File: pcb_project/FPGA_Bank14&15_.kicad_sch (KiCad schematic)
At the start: 16 parts, among them U1 XC7A100T-FTG256

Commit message: LED & FPGA_Started
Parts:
- removed C26: 330µF, symbol Device:C
- removed C27, C28, C29, C30, C31, C32: 4.7µF, symbol Device:C
- removed C33, C34, C35, C36, C37, C38, C39, C40: 0.47µF, symbol Device:C
- removed U1: XC7A100T-FTG256, symbol FPGA_Xilinx_Artix7:XC7A100T-FTG256
- added U7: XC7A100T-FTG256, symbol FPGA_Xilinx_Artix7:XC7A100T-FTG256
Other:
- removed sheet A_Bank14&15
- removed sheet B_Bank34&35

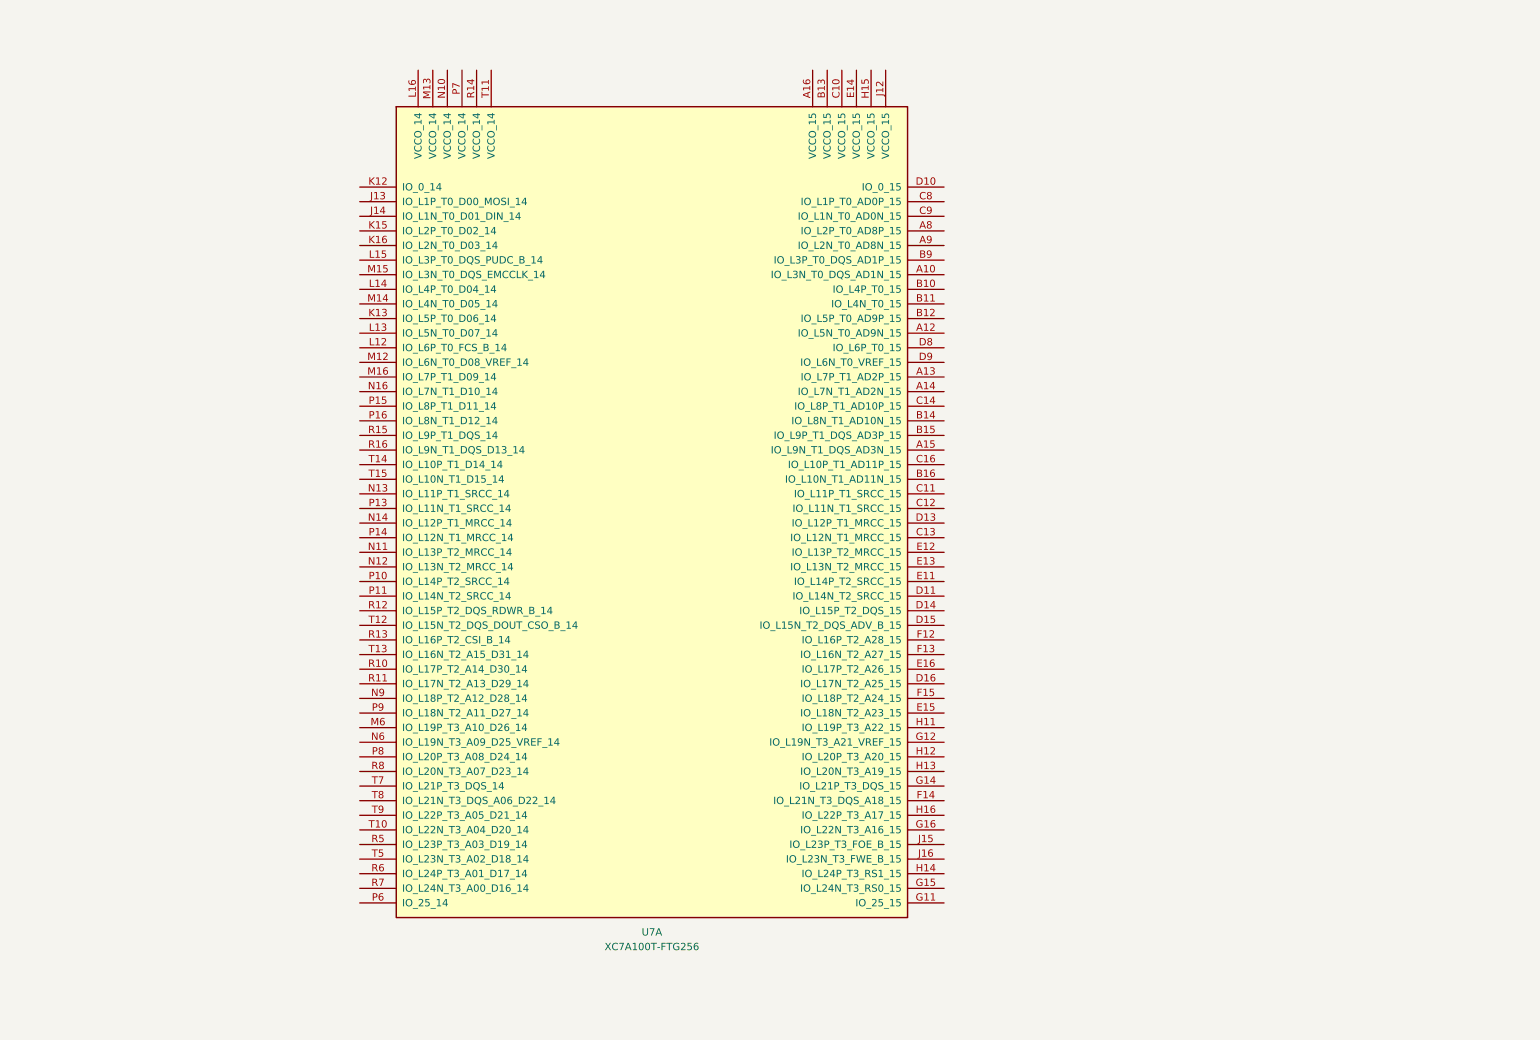
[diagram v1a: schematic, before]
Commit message: Crystal + SPI flash FPGA
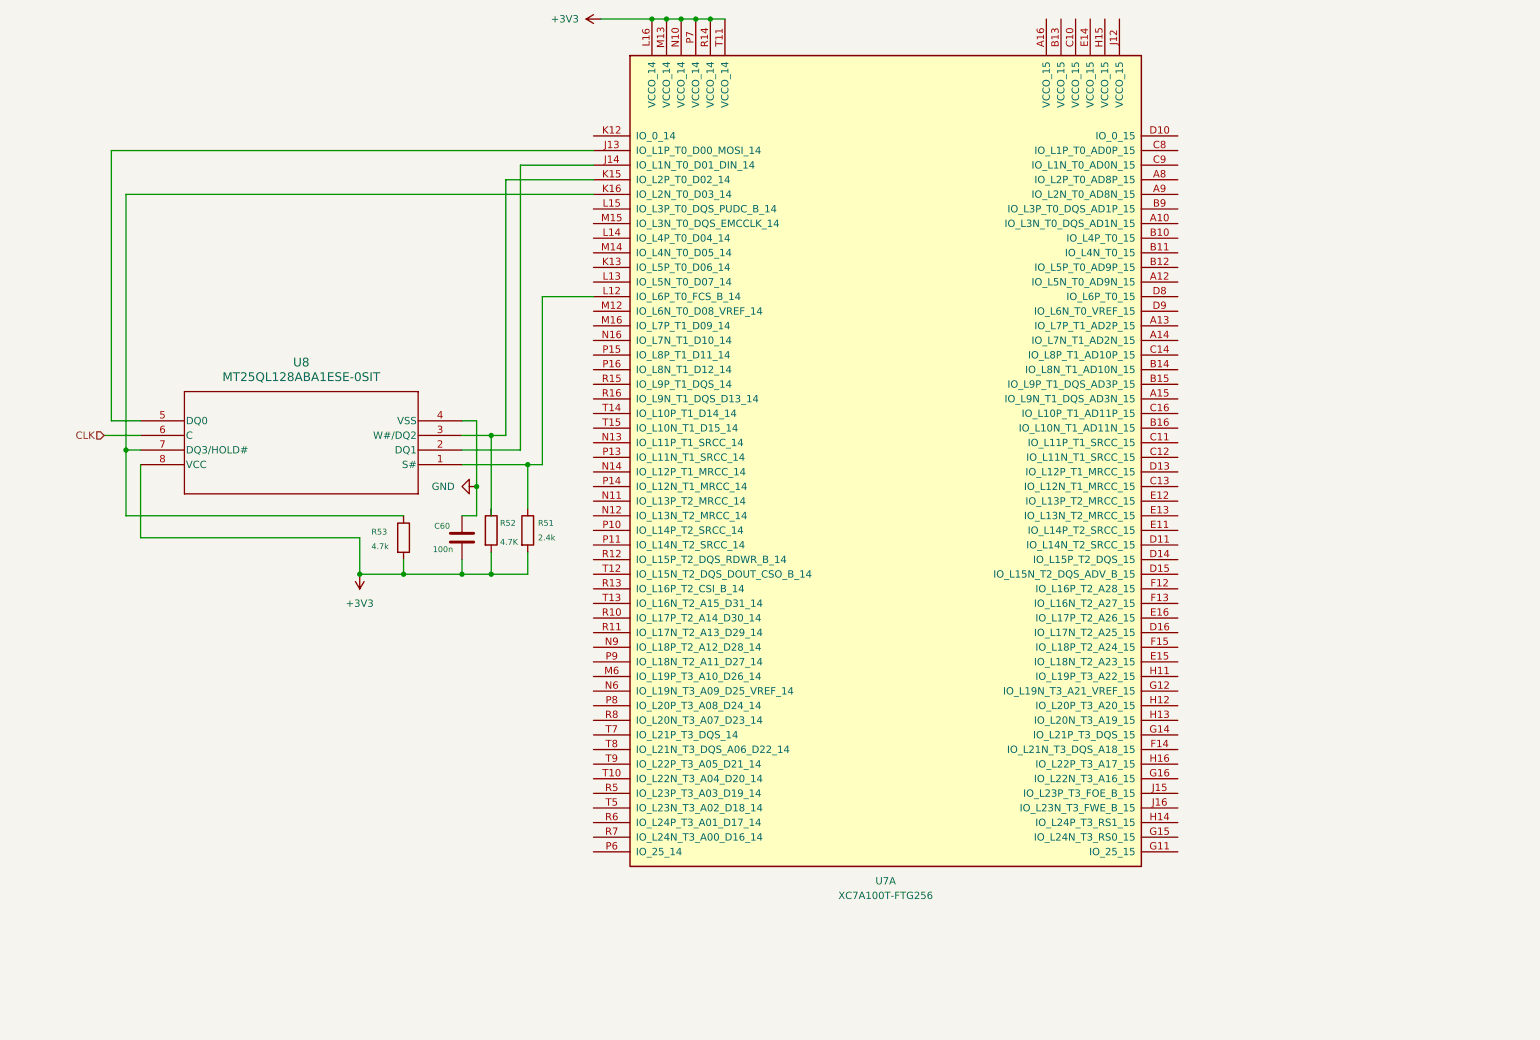
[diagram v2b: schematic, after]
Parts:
- added C60: 100n, symbol Device:C
- added R51: 2.4k, symbol Device:R
- added R52: 4.7K, symbol Device:R
- added R53: 4.7k, symbol Device:R
- added U8: MT25QL128ABA1ESE-0SIT, SOP2_8PIN_208MIL_MRN, symbol MT25QL128ABA1ESE_FPGAFLASH:MT25QL128ABA1ESE-0SIT
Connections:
- net at U7.J13 (IO_L1P_T0_D00_MOSI_14): now also U8.5 (DQ0)
- net at U7.J14 (IO_L1N_T0_D01_DIN_14): now also U8.2 (DQ1)
- net at U7.K15 (IO_L2P_T0_D02_14): now also U8.3 (W#/DQ2)
- net at U7.K16 (IO_L2N_T0_D03_14): now also R53.1, U8.7 (DQ3/HOLD#)
- net at U7.L12 (IO_L6P_T0_FCS_B_14): now also R51.1, U8.1 (S#)
- net +3V3: now reaches U7.L16 (VCCO_14)
- net +3V3: now also U7.M13 (VCCO_14), U7.N10 (VCCO_14), U7.P7 (VCCO_14), U7.R14 (VCCO_14), U7.T11 (VCCO_14), C60.2, R51.2, R52.2, R53.2, U8.8 (VCC)
- new net CLK: U8.6 (C)
- new net GND: C60.1, U8.4 (VSS)
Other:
- moved on the sheet: U7A

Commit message: Add framebuffer SRAM
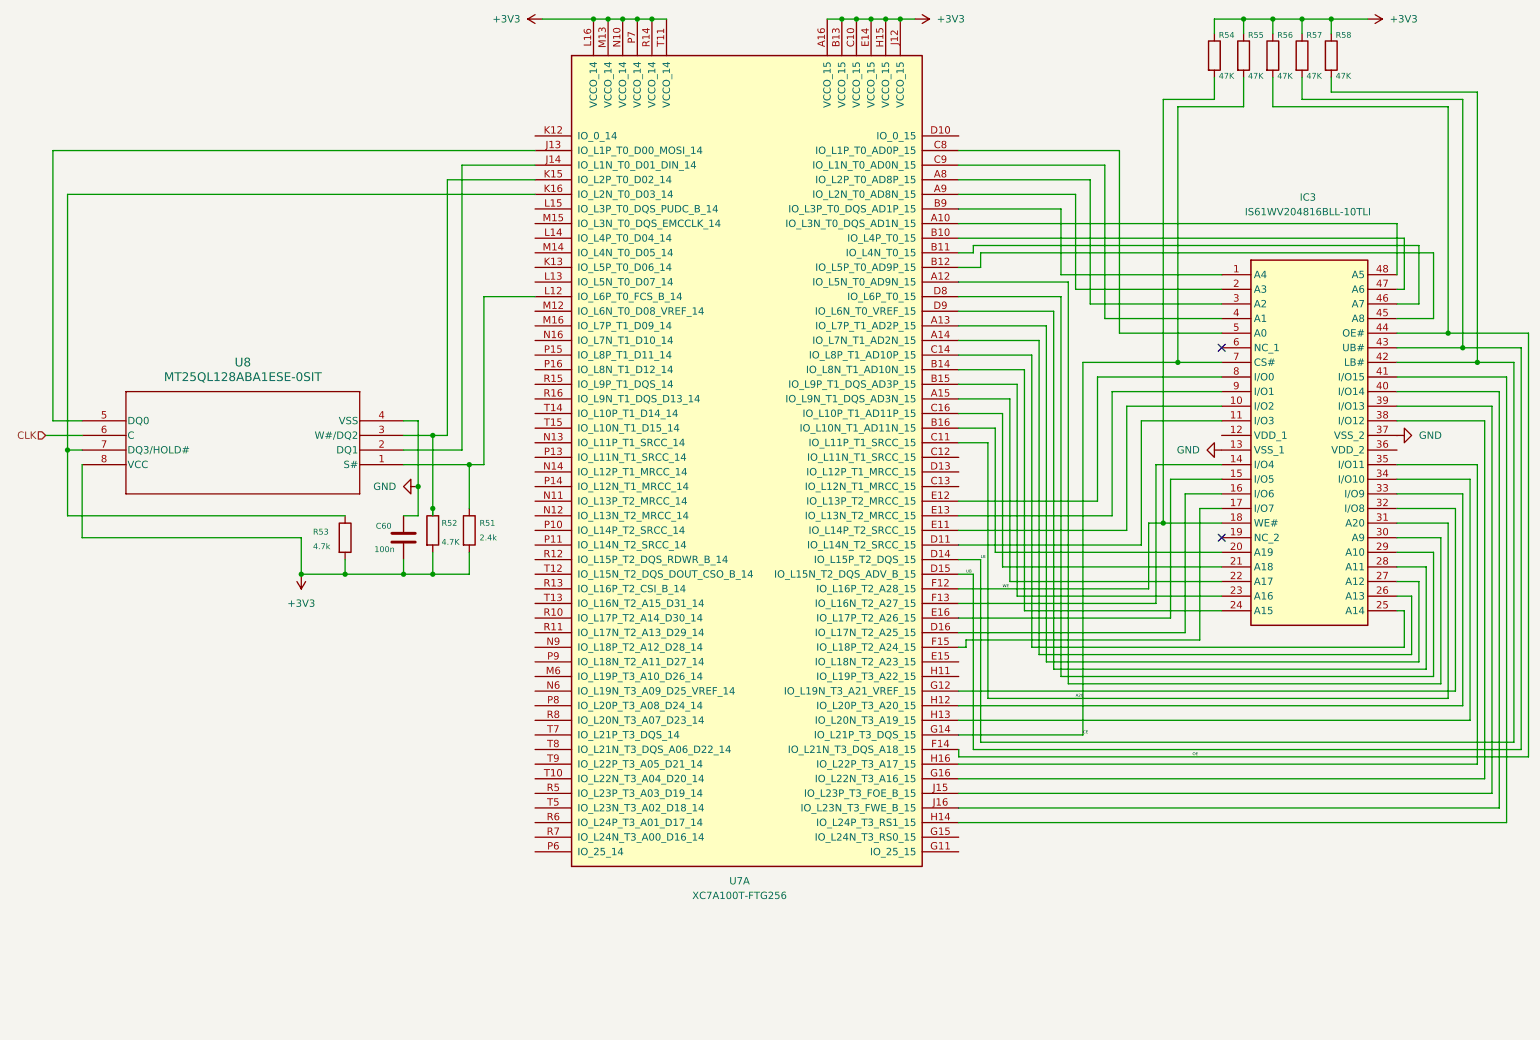
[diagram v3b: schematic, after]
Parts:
- added IC3: IS61WV204816BLL-10TLI, SOP50P2000X120-48N, symbol IS61WV204816BLL-10TLI:IS61WV204816BLL-10TLI
- added R54, R55, R56, R57, R58: 47K, symbol Device:R
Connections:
- net +3V3: now also U7.A16 (VCCO_15), U7.B13 (VCCO_15), U7.C10 (VCCO_15), U7.E14 (VCCO_15), U7.H15 (VCCO_15), U7.J12 (VCCO_15), R54.1, R55.1, R56.1, R57.1, R58.1
- net GND: now also IC3.13 (VSS_1), IC3.37 (VSS_2)
- net at U7.A10 (IO_L3N_T0_DQS_AD1N_15): now also IC3.48 (A5)
- net at U7.A12 (IO_L5N_T0_AD9N_15): now also IC3.30 (A9)
- net at U7.A13 (IO_L7P_T1_AD2P_15): now also IC3.27 (A12)
- net at U7.A14 (IO_L7N_T1_AD2N_15): now also IC3.26 (A13)
- net at U7.A15 (IO_L9N_T1_DQS_AD3N_15): now also IC3.22 (A17)
- net at U7.A8 (IO_L2P_T0_AD8P_15): now also IC3.3 (A2)
- net at U7.A9 (IO_L2N_T0_AD8N_15): now also IC3.2 (A3)
- net at U7.B10 (IO_L4P_T0_15): now also IC3.47 (A6)
- net at U7.B11 (IO_L4N_T0_15): now also IC3.46 (A7)
- net at U7.B12 (IO_L5P_T0_AD9P_15): now also IC3.45 (A8)
- net at U7.B14 (IO_L8N_T1_AD10N_15): now also IC3.24 (A15)
- net at U7.B15 (IO_L9P_T1_DQS_AD3P_15): now also IC3.23 (A16)
- net at U7.B16 (IO_L10N_T1_AD11N_15): now also IC3.20 (A19)
- net at U7.B9 (IO_L3P_T0_DQS_AD1P_15): now also IC3.1 (A4)
- net A20: now reaches U7.C11 (IO_L11P_T1_SRCC_15)
- net A20: now also IC3.31 (A20)
- net at U7.C14 (IO_L8P_T1_AD10P_15): now also IC3.25 (A14)
- net at U7.C16 (IO_L10P_T1_AD11P_15): now also IC3.21 (A18)
- net at U7.C8 (IO_L1P_T0_AD0P_15): now also IC3.5 (A0)
- net at U7.C9 (IO_L1N_T0_AD0N_15): now also IC3.4 (A1)
- net at U7.D11 (IO_L14N_T2_SRCC_15): now also IC3.11 (I/O3)
- net LB: now reaches U7.D14 (IO_L15P_T2_DQS_15)
- net LB: now also IC3.42 (LB#), R58.2
- net UB: now reaches U7.D15 (IO_L15N_T2_DQS_ADV_B_15)
- net UB: now also IC3.43 (UB#), R57.2
- net at U7.D16 (IO_L17N_T2_A25_15): now also IC3.16 (I/O6)
- net at U7.D8 (IO_L6P_T0_15): now also IC3.29 (A10)
- net at U7.D9 (IO_L6N_T0_VREF_15): now also IC3.28 (A11)
- net at U7.E11 (IO_L14P_T2_SRCC_15): now also IC3.10 (I/O2)
- net at U7.E12 (IO_L13P_T2_MRCC_15): now also IC3.8 (I/O0)
- net at U7.E13 (IO_L13N_T2_MRCC_15): now also IC3.9 (I/O1)
- net at U7.E16 (IO_L17P_T2_A26_15): now also IC3.15 (I/O5)
- net WE: now reaches U7.F12 (IO_L16P_T2_A28_15)
- net WE: now also IC3.18 (WE#), R54.2
- net at U7.F13 (IO_L16N_T2_A27_15): now also IC3.14 (I/O4)
- net OE: now reaches U7.F14 (IO_L21N_T3_DQS_A18_15)
- net OE: now also IC3.44 (OE#), R56.2
- net at U7.F15 (IO_L18P_T2_A24_15): now also IC3.17 (I/O7)
- net at U7.G12 (IO_L19N_T3_A21_VREF_15): now also IC3.32 (I/O8)
- net CE: now reaches U7.G14 (IO_L21P_T3_DQS_15)
- net CE: now also IC3.7 (CS#), R55.2
- net at U7.G16 (IO_L22N_T3_A16_15): now also IC3.38 (I/O12)
- net at U7.H12 (IO_L20P_T3_A20_15): now also IC3.33 (I/O9)
- net at U7.H13 (IO_L20N_T3_A19_15): now also IC3.34 (I/O10)
- net at U7.H14 (IO_L24P_T3_RS1_15): now also IC3.41 (I/O15)
- net at U7.H16 (IO_L22P_T3_A17_15): now also IC3.35 (I/O11)
- net at U7.J15 (IO_L23P_T3_FOE_B_15): now also IC3.39 (I/O13)
- net at U7.J16 (IO_L23N_T3_FWE_B_15): now also IC3.40 (I/O14)
- net at U7.K15 (IO_L2P_T0_D02_14), U8.3 (W#/DQ2): now also R52.1
- no-connect marks 0 -> 2
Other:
- moved on the sheet: C60, R51, R52, R53, U7A, U8

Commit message: Add FPGA JTAG
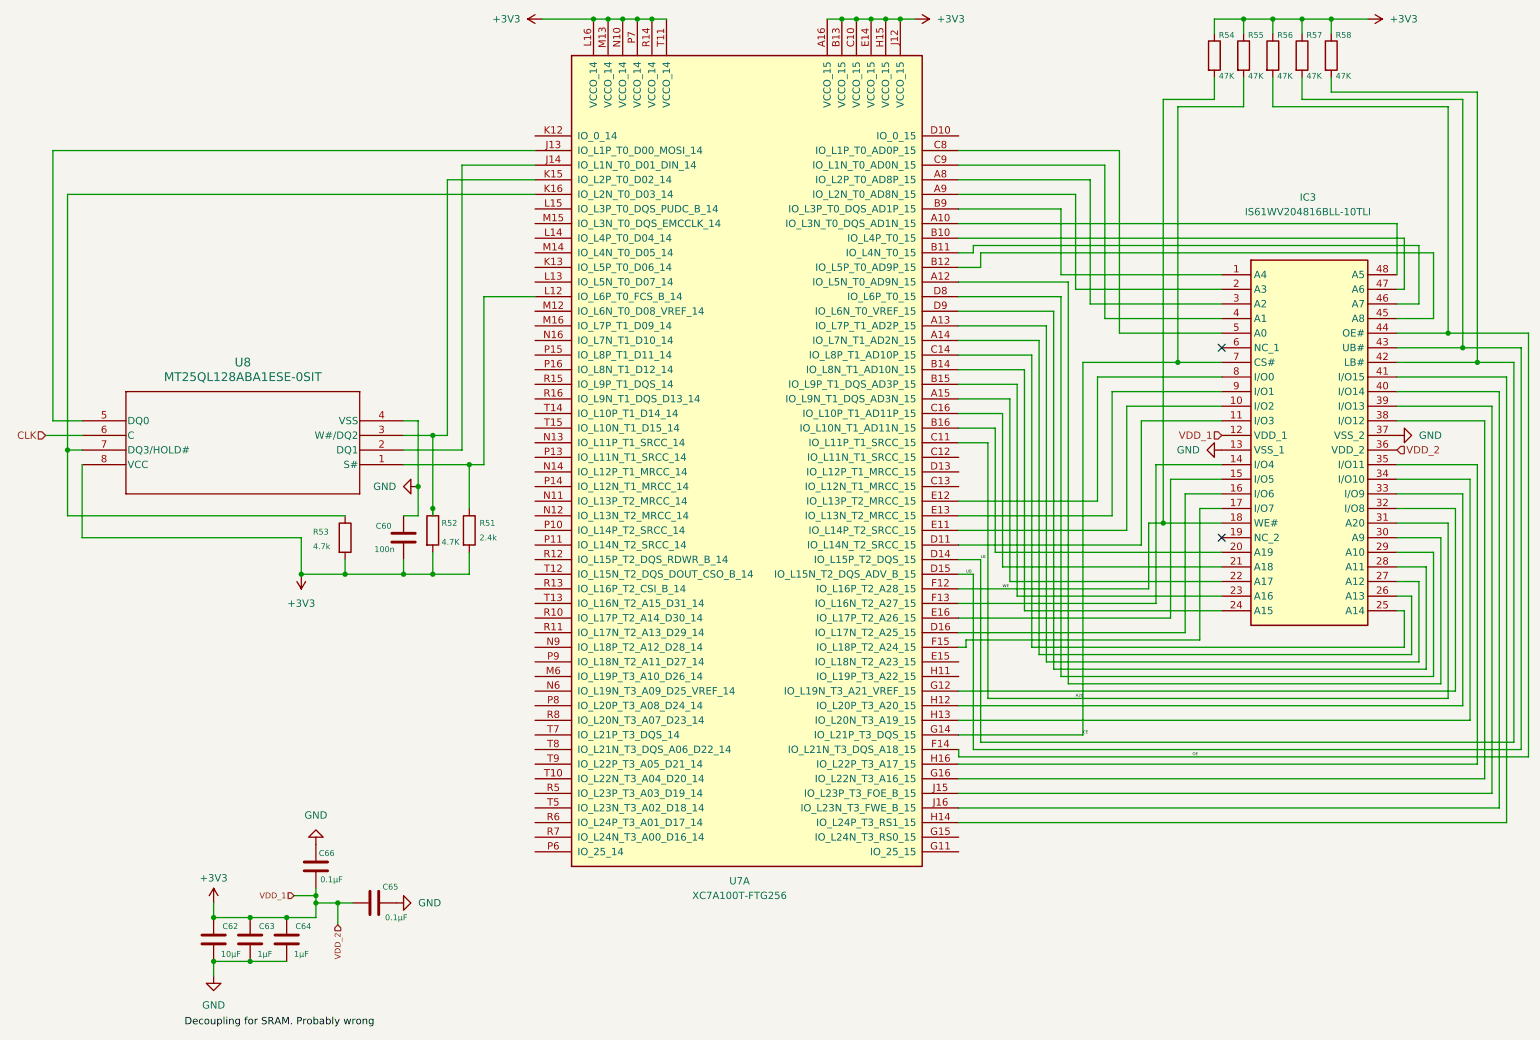
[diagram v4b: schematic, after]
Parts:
- added C62: 10µF, symbol Device:C
- added C63, C64: 1µF, symbol Device:C
- added C65, C66: 0.1µF, symbol Device:C
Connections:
- net +3V3: now also IC3.12 (VDD_1), IC3.36 (VDD_2), C62.1, C63.1, C64.1, C65.1, C66.2
- net GND: now also C62.2, C63.2, C64.2, C65.2, C66.1
